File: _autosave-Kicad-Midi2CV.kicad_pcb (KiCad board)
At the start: 2 copper layers, 99.7 x 99.7 mm, 84 parts, among them IC1 MCP4725module, IC2 MCP4725module, J1 Doepfer connector, J10 CV4, J11 Gate1, J12 GateConn, J13 Gate2, J14 Gate3, J15 Gate4, J16 I2C_Conn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

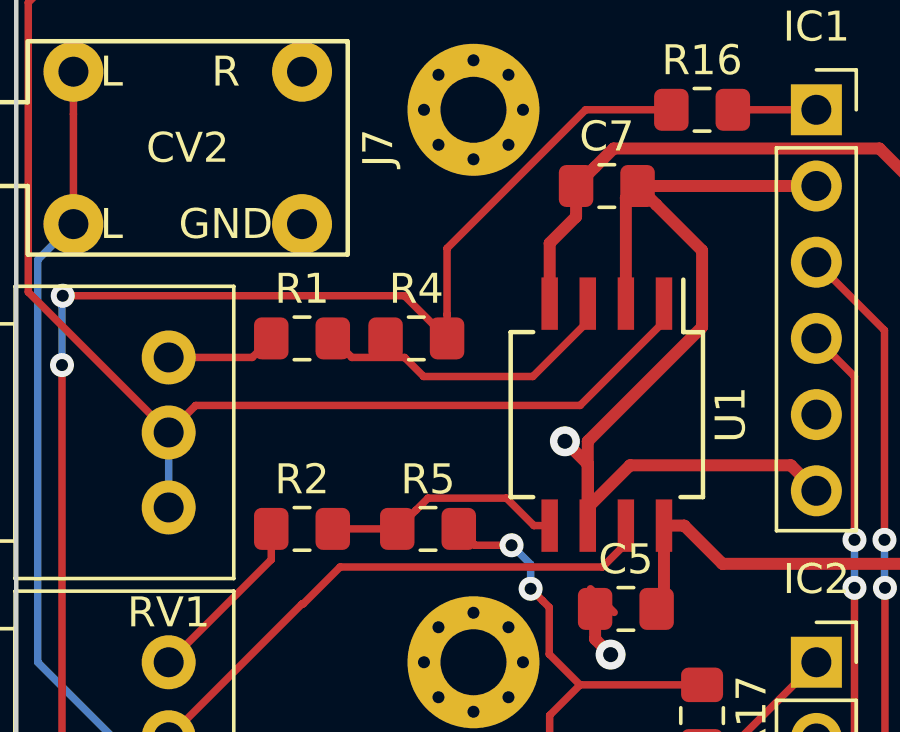
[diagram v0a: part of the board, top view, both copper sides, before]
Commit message: AJ_SO8 pad for Op Amp
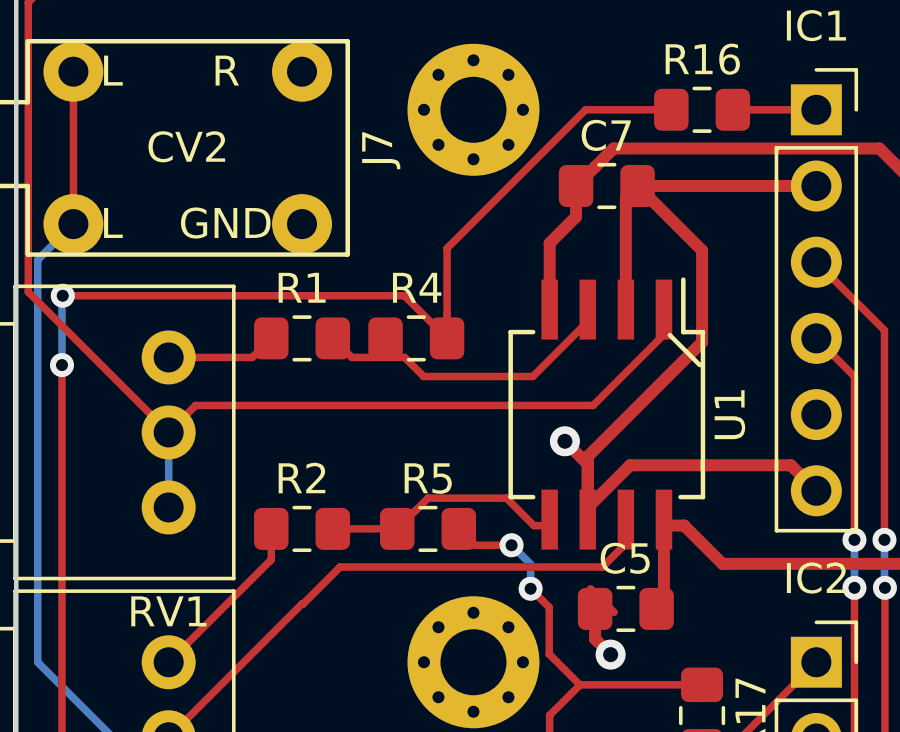
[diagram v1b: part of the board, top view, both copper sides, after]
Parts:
- U1: footprint Package_SO:SO-8_5.3x6.2mm_P1.27mm -> AJ-Dropbox-Kicad:AJ_SO-8_5.3x6.2mm_P1.27mm
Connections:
- R4 pad 2: CV1 -> GND
- R5 pad 2: CV2 -> GND
- U1 pad 2: GND -> Net-(R1-Pad2)
- U1 pad 3: Net-(R1-Pad2) -> CV1
- U1 pad 5: Net-(R2-Pad2) -> CV2
- U1 pad 6: GND -> Net-(R2-Pad2)
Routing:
- net GND: track 81.1 -> 81.6 mm
